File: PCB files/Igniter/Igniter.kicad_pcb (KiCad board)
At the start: 2 copper layers, 124.9 x 69.6 mm, 57 parts, among them IC1 74HC4050, J1 PT, J10 SL3, J11 SL4, J12 SL5, J13 Micro_SD_Card, J2 PT, J3 PT, J4 PT, J5 Battery, J6 COIL, J7 COIL, J8 SL1, J9 SL2, Q1 IGN, Q2 Q_NMOS_GDSD, Q3 Q_NMOS_GDSD, Q4 Q_NMOS_GDSD, Q5 Q_NMOS_GDSD, Q6 Q_NMOS_GDSD, SW1 ARM, U2 FDS8984, U3 FDS8984, U4 FDS8984

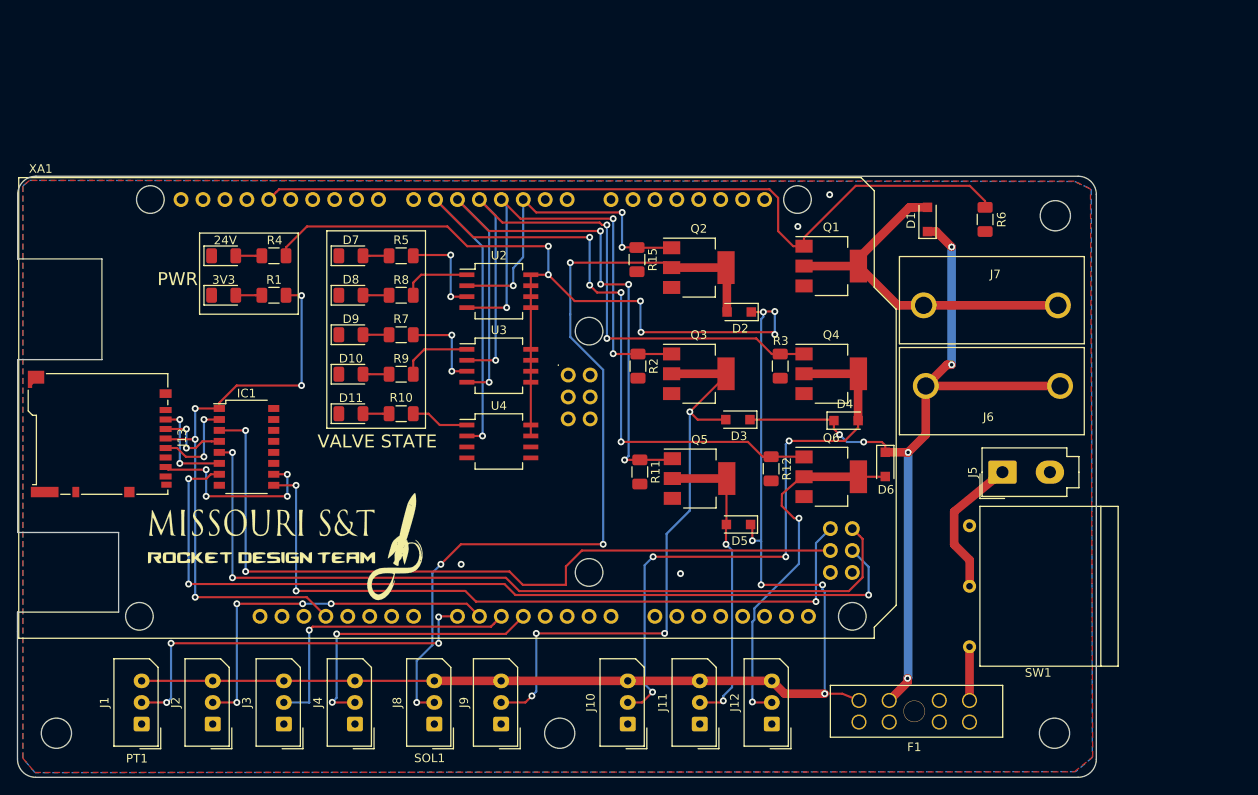
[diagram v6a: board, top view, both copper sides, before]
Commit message: 1/19/2020
-Added filled zones at fuse connections
Note: read netlist and created duplicate footprints, all were deleted and no nets seemed to be affected
-Added more label text on silkscreen layer
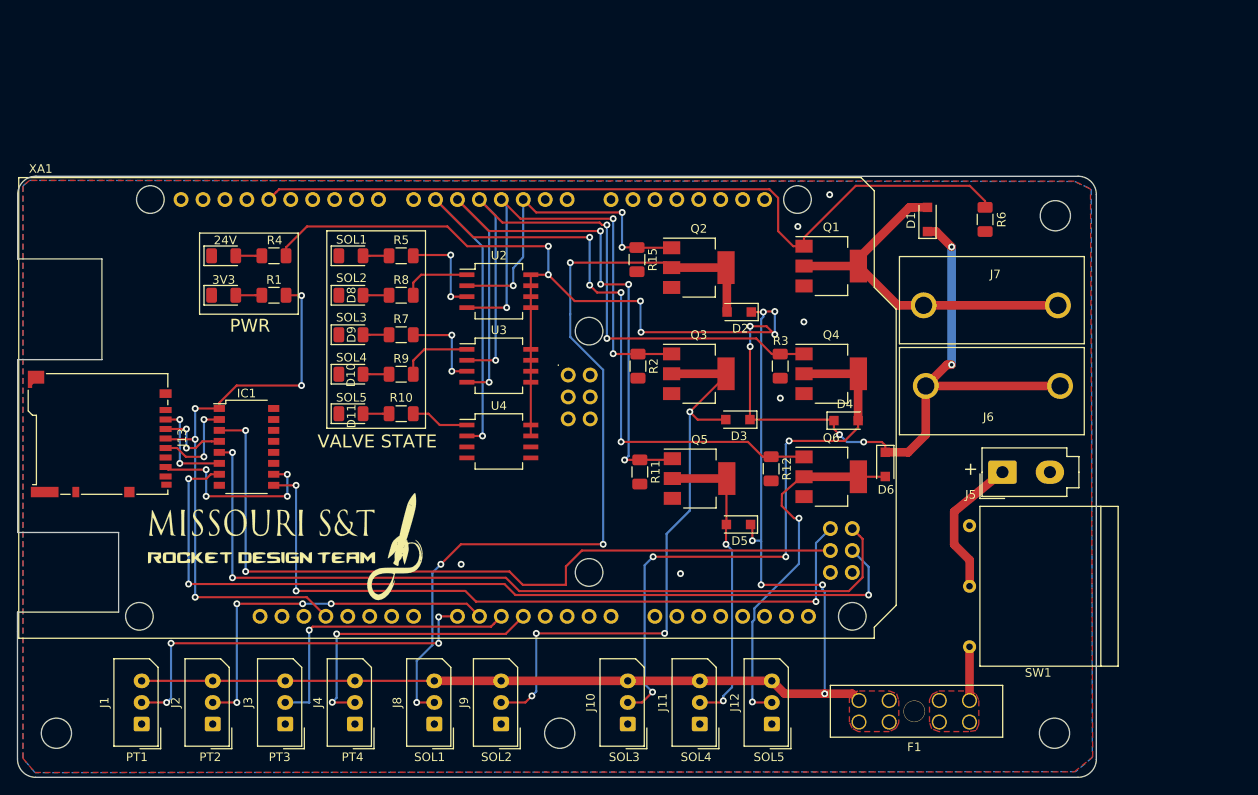
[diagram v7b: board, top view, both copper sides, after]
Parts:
- moved J3 0.16 mm to (116.1, 149.6)
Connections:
- XA1 pad GND3: Net-(XA1-PadGND3) -> Net-(XA1-PadGND2)
- XA1 pad GND5: Net-(XA1-PadGND5) -> Net-(XA1-PadGND2)
- XA1 pad GND6: Net-(XA1-PadGND5) -> Net-(XA1-PadGND2)
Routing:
- net +24V: track 328.0 -> 313.6 mm
- net GNDREF: vias 4 -> 6
- added copper zone on F.Cu, net +24V
- added copper zone on F.Cu, net Net-(F1-Pad5)
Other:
- board text added: "+"
- board text added: "PT2"
- board text added: "PT3"
- board text added: "PT4"
- board text added: "SOL2"
- board text added: "SOL3"
- board text added: "SOL4"
- board text added: "SOL5"

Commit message: 1/20/2020
-Fixed ground connections being seperated
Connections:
- XA1 pad GND2: Net-(XA1-PadGND2) -> GNDREF
- XA1 pad GND3: Net-(XA1-PadGND2) -> GNDREF
- XA1 pad GND5: Net-(XA1-PadGND2) -> GNDREF
- XA1 pad GND6: Net-(XA1-PadGND2) -> GNDREF
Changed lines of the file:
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@@
     (zones 0)
     (modules 57)
-    (nets 100)
+    (nets 99)
   )
   (page A4)
@@
       (padsonsilk false)
       (subtractmaskfromsilk false)
-      (outputformat 1)
+      (outputformat 4)
       (mirror false)
       (drillshape 0)
       (scaleselection 1)
-      (outputdirectory "gerbs/"))
+      (outputdirectory "Renders/"))
   )
   (net 0 "")
@@
   (net 86 "Net-(XA1-PadRST1)")
   (net 87 "Net-(XA1-Pad5V1)")
-  (net 88 "Net-(XA1-PadGND2)")
-  (net 89 "Net-(XA1-PadVIN)")
-  (net 90 "Net-(XA1-Pad5V2)")
-  (net 91 "Net-(XA1-PadSCK)")
-  (net 92 "Net-(XA1-PadMOSI)")
-  (net 93 "Net-(XA1-PadRST2)")
-  (net 94 /SPRK)
-  (net 95 /SOL1)
-  (net 96 /SOL2)
-  (net 97 /SOL3)
-  (net 98 /SOL4)
-  (net 99 /SOL5)
+  (net 88 "Net-(XA1-PadVIN)")
+  (net 89 "Net-(XA1-Pad5V2)")
+  (net 90 "Net-(XA1-PadSCK)")
+  (net 91 "Net-(XA1-PadMOSI)")
+  (net 92 "Net-(XA1-PadRST2)")
+  (net 93 /SPRK)
+  (net 94 /SOL1)
+  (net 95 /SOL2)
+  (net 96 /SOL3)
+  (net 97 /SOL4)
+  (net 98 /SOL5)
   (net_class Default "This is the default net class."
     (clearance 0.2)
@@
     (add_net "Net-(XA1-PadD8)")
     (add_net "Net-(XA1-PadD9)")
-    (add_net "Net-(XA1-PadGND2)")
     (add_net "Net-(XA1-PadIORF)")
     (add_net "Net-(XA1-PadMISO)")
@@
       (net 53 "Net-(XA1-PadMISO)"))
     (pad GND6 thru_hole oval (at 96.52 -7.62) (size 1.7272 1.7272) (drill 1.016) (layers *.Cu *.Mask)
-      (net 88 "Net-(XA1-PadGND2)"))
+      (net 2 GNDREF))
     (pad GND5 thru_hole oval (at 93.98 -7.62) (size 1.7272 1.7272) (drill 1.016) (layers *.Cu *.Mask)
-      (net 88 "Net-(XA1-PadGND2)"))
+      (net 2 GNDREF))
     (pad D53 thru_hole oval (at 96.52 -10.16) (size 1.7272 1.7272) (drill 1.016) (layers *.Cu *.Mask)
       (net 27 /CS))
@@
       (net 67 "Net-(XA1-PadD12)"))
     (pad D13 thru_hole oval (at 28.956 -50.8) (size 1.7272 1.7272) (drill 1.016) (layers *.Cu *.Mask)
-      (net 94 /SPRK))
+      (net 93 /SPRK))
     (pad AREF thru_hole oval (at 23.876 -50.8) (size 1.7272 1.7272) (drill 1.016) (layers *.Cu *.Mask)
       (net 68 "Net-(XA1-PadAREF)"))
@@
       (net 74 "Net-(XA1-PadD7)"))
     (pad D6 thru_hole oval (at 48.26 -50.8) (size 1.7272 1.7272) (drill 1.016) (layers *.Cu *.Mask)
-      (net 99 /SOL5))
+      (net 98 /SOL5))
     (pad D5 thru_hole oval (at 50.8 -50.8) (size 1.7272 1.7272) (drill 1.016) (layers *.Cu *.Mask)
-      (net 98 /SOL4))
+      (net 97 /SOL4))
     (pad D4 thru_hole oval (at 53.34 -50.8) (size 1.7272 1.7272) (drill 1.016) (layers *.Cu *.Mask)
-      (net 97 /SOL3))
+      (net 96 /SOL3))
     (pad D3 thru_hole oval (at 55.88 -50.8) (size 1.7272 1.7272) (drill 1.016) (layers *.Cu *.Mask)
-      (net 96 /SOL2))
+      (net 95 /SOL2))
     (pad D2 thru_hole oval (at 58.42 -50.8) (size 1.7272 1.7272) (drill 1.016) (layers *.Cu *.Mask)
-      (net 95 /SOL1))
+      (net 94 /SOL1))
     (pad D1 thru_hole oval (at 60.96 -50.8) (size 1.7272 1.7272) (drill 1.016) (layers *.Cu *.Mask)
       (net 75 "Net-(XA1-PadD1)"))
@@
       (net 87 "Net-(XA1-Pad5V1)"))
     (pad GND2 thru_hole oval (at 40.64 -2.54) (size 1.7272 1.7272) (drill 1.016) (layers *.Cu *.Mask)
-      (net 88 "Net-(XA1-PadGND2)"))
+      (net 2 GNDREF))
     (pad GND3 thru_hole oval (at 43.18 -2.54) (size 1.7272 1.7272) (drill 1.016) (layers *.Cu *.Mask)
-      (net 88 "Net-(XA1-PadGND2)"))
+      (net 2 GNDREF))
     (pad VIN thru_hole oval (at 45.72 -2.54) (size 1.7272 1.7272) (drill 1.016) (layers *.Cu *.Mask)
-      (net 89 "Net-(XA1-PadVIN)"))
+      (net 88 "Net-(XA1-PadVIN)"))
     (pad A0 thru_hole oval (at 50.8 -2.54) (size 1.7272 1.7272) (drill 1.016) (layers *.Cu *.Mask)
       (net 33 /PT0))
     (pad 5V2 thru_hole oval (at 66.167 -30.48) (size 1.7272 1.7272) (drill 1.016) (layers *.Cu *.Mask)
-      (net 90 "Net-(XA1-Pad5V2)"))
+      (net 89 "Net-(XA1-Pad5V2)"))
     (pad SCK thru_hole oval (at 63.627 -27.94) (size 1.7272 1.7272) (drill 1.016) (layers *.Cu *.Mask)
-      (net 91 "Net-(XA1-PadSCK)"))
+      (net 90 "Net-(XA1-PadSCK)"))
     (pad MOSI thru_hole oval (at 66.167 -27.94) (size 1.7272 1.7272) (drill 1.016) (layers *.Cu *.Mask)
-      (net 92 "Net-(XA1-PadMOSI)"))
+      (net 91 "Net-(XA1-PadMOSI)"))
     (pad GND4 thru_hole oval (at 66.167 -25.4) (size 1.7272 1.7272) (drill 1.016) (layers *.Cu *.Mask)
       (net 2 GNDREF))
     (pad RST2 thru_hole oval (at 63.627 -25.4) (size 1.7272 1.7272) (drill 1.016) (layers *.Cu *.Mask)
-      (net 93 "Net-(XA1-PadRST2)"))
+      (net 92 "Net-(XA1-PadRST2)"))
   )
   (module Diode_SMD:D_SOD-123F (layer F.Cu)
@@
     (fp_line (start -1.6 0.8) (end -1.6 -0.8) (layer F.Fab) (width 0.1))
     (pad 2 smd roundrect (at 1.4 0 90) (size 1.25 1.75) (layers F.Cu F.Paste F.Mask) (roundrect_rratio 0.2)
-      (net 94 /SPRK))
+      (net 93 /SPRK))
     (pad 1 smd roundrect (at -1.4 0 90) (size 1.25 1.75) (layers F.Cu F.Paste F.Mask) (roundrect_rratio 0.2)
       (net 2 GNDREF))
@@
       (net 2 GNDREF))
     (pad 1 smd rect (at -3.15 -2.3) (size 2 1.5) (layers F.Cu F.Paste F.Mask)
-      (net 94 /SPRK))
+      (net 93 /SPRK))
     (model ${KISYS3DMOD}/Package_TO_SOT_SMD.3dshapes/SOT-223.wrl
       (at (xyz 0 0 0))
@@
   (gr_line (start 87.1855 155.7274) (end 207.8863 155.7274) (layer Edge.Cuts) (width 0.05))
   (gr_line (start 85.09 138.8364) (end 85.089797 153.606348) (layer Edge.Cuts) (width 0.05))
-  (via (at 173.4185 111.8235) (size 0.8) (drill 0.4) (layers F.Cu B.Cu) (net 2))
   (segment (start 190.1375 101.0793) (end 205.6875 101.0793) (width 1) (layer F.Cu) (net 1))
   (segment (start 176.1613 96.5327) (end 182.4613 96.5327) (width 1) (layer F.Cu) (net 1))
@@
   (segment (start 187.0079 101.0793) (end 182.4613 96.5327) (width 1) (layer F.Cu) (net 1))
   (segment (start 190.0125 101.0793) (end 187.0079 101.0793) (width 1) (layer F.Cu) (net 1))
+  (via (at 173.4185 111.8235) (size 0.8) (drill 0.4) (layers F.Cu B.Cu) (net 2))
   (via (at 136.4615 131.064) (size 0.8) (drill 0.4) (layers F.Cu B.Cu) (net 2))
   (via (at 161.8615 132.1435) (size 0.8) (drill 0.4) (layers F.Cu B.Cu) (net 2))
@@
   (segment (start 177.546 128.59766) (end 179.21478 126.92888) (width 0.25) (layer B.Cu) (net 40))
   (segment (start 177.546 135.382) (end 177.546 128.59766) (width 0.25) (layer B.Cu) (net 40))
-  (segment (start 174.9113 94.2327) (end 173.1645 92.4859) (width 0.25) (layer F.Cu) (net 94))
-  (segment (start 176.1613 94.2327) (end 174.9113 94.2327) (width 0.25) (layer F.Cu) (net 94))
-  (segment (start 115.054379 87.965281) (end 114.19078 88.82888) (width 0.25) (layer F.Cu) (net 94))
-  (segment (start 115.379381 87.640279) (end 115.054379 87.965281) (width 0.25) (layer F.Cu) (net 94))
-  (segment (start 172.165309 87.640279) (end 115.379381 87.640279) (width 0.25) (layer F.Cu) (net 94))
-  (segment (start 173.1645 88.63947) (end 172.165309 87.640279) (width 0.25) (layer F.Cu) (net 94))
-  (segment (start 173.1645 92.4859) (end 173.1645 88.63947) (width 0.25) (layer F.Cu) (net 94))
-  (segment (start 176.1613 93.2327) (end 176.1613 94.2327) (width 0.25) (layer F.Cu) (net 94))
-  (segment (start 182.1577 87.2363) (end 176.1613 93.2327) (width 0.25) (layer F.Cu) (net 94))
-  (segment (start 195.3555 87.2363) (end 182.1577 87.2363) (width 0.25) (layer F.Cu) (net 94))
-  (segment (start 197.1294 89.7352) (end 197.1294 89.0102) (width 0.25) (layer F.Cu) (net 94))
-  (segment (start 197.1294 89.0102) (end 195.3555 87.2363) (width 0.25) (layer F.Cu) (net 94))
+  (segment (start 174.9113 94.2327) (end 173.1645 92.4859) (width 0.25) (layer F.Cu) (net 93))
+  (segment (start 176.1613 94.2327) (end 174.9113 94.2327) (width 0.25) (layer F.Cu) (net 93))
+  (segment (start 115.054379 87.965281) (end 114.19078 88.82888) (width 0.25) (layer F.Cu) (net 93))
+  (segment (start 115.379381 87.640279) (end 115.054379 87.965281) (width 0.25) (layer F.Cu) (net 93))
+  (segment (start 172.165309 87.640279) (end 115.379381 87.640279) (width 0.25) (layer F.Cu) (net 93))
+  (segment (start 173.1645 88.63947) (end 172.165309 87.640279) (width 0.25) (layer F.Cu) (net 93))
+  (segment (start 173.1645 92.4859) (end 173.1645 88.63947) (width 0.25) (layer F.Cu) (net 93))
+  (segment (start 176.1613 93.2327) (end 176.1613 94.2327) (width 0.25) (layer F.Cu) (net 93))
+  (segment (start 182.1577 87.2363) (end 176.1613 93.2327) (width 0.25) (layer F.Cu) (net 93))
+  (segment (start 195.3555 87.2363) (end 182.1577 87.2363) (width 0.25) (layer F.Cu) (net 93))
+  (segment (start 197.1294 89.7352) (end 197.1294 89.0102) (width 0.25) (layer F.Cu) (net 93))
+  (segment (start 197.1294 89.0102) (end 195.3555 87.2363) (width 0.25) (layer F.Cu) (net 93))
   (zone (net 2) (net_name GNDREF) (layer F.Cu) (hatch edge 0.508)
     (connect_pads yes (clearance 0.508))
     (min_thickness 0.254)
-    (fill (arc_segments 32) (thermal_gap 0.508) (thermal_bridge_width 0.508))
+    (fill yes (arc_segments 32) (thermal_gap 0.508) (thermal_bridge_width 0.508))
     (polygon
       (pts
@@
     (connect_pads yes (clearance 0.508))
     (min_thickness 0.254)
-    (fill (arc_segments 32) (thermal_gap 0.508) (thermal_bridge_width 0.508))
+    (fill yes (arc_segments 32) (thermal_gap 0.508) (thermal_bridge_width 0.508))
     (polygon
       (pts
@@
     (connect_pads yes (clearance 0.508))
     (min_thickness 0.254)
-    (fill (arc_segments 32) (thermal_gap 0.508) (thermal_bridge_width 0.508) (smoothing fillet))
+    (fill yes (arc_segments 32) (thermal_gap 0.508) (thermal_bridge_width 0.508) (smoothing fillet))
     (polygon
       (pts
@@
     (connect_pads yes (clearance 0.508))
     (min_thickness 0.254)
-    (fill (arc_segments 32) (thermal_gap 0.508) (thermal_bridge_width 0.508) (smoothing fillet))
+    (fill yes (arc_segments 32) (thermal_gap 0.508) (thermal_bridge_width 0.508) (smoothing fillet))
     (polygon
       (pts
